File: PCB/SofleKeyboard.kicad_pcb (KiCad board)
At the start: 2 copper layers, 137.2 x 109.2 mm, 87 parts, among them J1 LED, J2 4PIN, J3 OLED, P1 i2c_pin, P2 i2c_pin, SW1 SW_PUSH, SW10 SW_PUSH, SW11 SW_PUSH, SW12 SW_PUSH, SW13 SW_PUSH, SW14 SW_PUSH, SW15 SW_PUSH, SW16 SW_PUSH, SW17 SW_PUSH, SW18 SW_PUSH, SW19 SW_PUSH, SW2 SW_PUSH, SW20 SW_PUSH, SW21 SW_PUSH, SW22 SW_PUSH, SW23 SW_PUSH, SW24 SW_PUSH, SW25 Rotary_Encoder_Switch, SW26 SW_PUSH, SW27 SW_PUSH, SW28 SW_PUSH, SW29 SW_PUSH, SW3 SW_PUSH, SW30 SW_PUSH, SW4 SW_PUSH, SW5 SW_PUSH, SW6 SW_PUSH, SW7 SW_PUSH, SW8 SW_PUSH, SW9 SW_PUSH, U1 ProMicro

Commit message: Finishing touches before ordering
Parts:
- moved Ref** 1.70 mm to (96.8, 124.6)
- moved Ref** 1.42 mm to (95.8, 124.5)
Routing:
- net ENCA: track 73.0 -> 69.0 mm
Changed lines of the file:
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@@
     (thickness 1.6)
     (drawings 193)
-    (tracks 1892)
+    (tracks 1886)
     (zones 0)
     (modules 87)
@@
     (0 F.Cu signal)
     (31 B.Cu signal)
-    (32 B.Adhes user hide)
-    (33 F.Adhes user hide)
-    (34 B.Paste user hide)
-    (35 F.Paste user hide)
+    (32 B.Adhes user)
+    (33 F.Adhes user)
+    (34 B.Paste user)
+    (35 F.Paste user)
     (36 B.SilkS user)
     (37 F.SilkS user)
-    (38 B.Mask user hide)
-    (39 F.Mask user hide)
-    (40 Dwgs.User user hide)
-    (41 Cmts.User user hide)
-    (42 Eco1.User user hide)
+    (38 B.Mask user)
+    (39 F.Mask user)
+    (40 Dwgs.User user)
+    (41 Cmts.User user)
+    (42 Eco1.User user)
     (43 Eco2.User user)
     (44 Edge.Cuts user)
-    (45 Margin user hide)
-    (46 B.CrtYd user hide)
-    (47 F.CrtYd user hide)
-    (48 B.Fab user hide)
-    (49 F.Fab user hide)
+    (45 Margin user)
+    (46 B.CrtYd user)
+    (47 F.CrtYd user)
+    (48 B.Fab user)
+    (49 F.Fab user)
   )
   (setup
@@
   )
   (module SofleKeyboard-footprint:SofleLogoSmall (layer B.Cu)
-    (at 96.58 125.74 180)
+    (at 95.81 124.55 180)
     (fp_text reference Ref** (at 0 0) (layer B.SilkS) hide
       (effects (font (size 1.27 1.27) (thickness 0.15)) (justify mirror))
@@
   )
   (module SofleKeyboard-footprint:SofleLogoSmall (layer F.Cu)
-    (at 97.92 125.86)
+    (at 96.77 124.61)
     (fp_text reference Ref** (at 0 0) (layer F.SilkS) hide
       (effects (font (size 1.27 1.27) (thickness 0.15)))
@@
   (segment (start 98.514255 52.585745) (end 106.224255 52.585745) (width 0.25) (layer F.Cu) (net 56))
   (via (at 98.514255 52.585745) (size 0.4) (drill 0.3) (layers F.Cu B.Cu) (net 56))
-  (segment (start 93.499999 101.000001) (end 92.5 102) (width 0.25) (layer B.Cu) (net 56) (status 20))
+  (segment (start 93.499999 101.000001) (end 92.5 102) (width 0.25) (layer B.Cu) (net 56))
   (segment (start 101.37501 93.12499) (end 93.499999 101.000001) (width 0.25) (layer B.Cu) (net 56))
-  (segment (start 101.37501 87.263295) (end 101.37501 93.12499) (width 0.25) (layer B.Cu) (net 56))
-  (segment (start 98.913295 86.57499) (end 100.686705 86.57499) (width 0.25) (layer B.Cu) (net 56))
-  (segment (start 99.013275 86.47501) (end 98.913295 86.57499) (width 0.25) (layer B.Cu) (net 56))
-  (segment (start 101.37501 85.786705) (end 100.686705 86.47501) (width 0.25) (layer B.Cu) (net 56))
-  (segment (start 101.37501 84.563295) (end 101.37501 85.786705) (width 0.25) (layer B.Cu) (net 56))
-  (segment (start 98.216499 81.404784) (end 101.37501 84.563295) (width 0.25) (layer B.Cu) (net 56))
-  (segment (start 100.686705 86.57499) (end 101.37501 87.263295) (width 0.25) (layer B.Cu) (net 56))
-  (segment (start 98.216499 53.166343) (end 98.216499 81.404784) (width 0.25) (layer B.Cu) (net 56))
   (segment (start 98.514255 52.868587) (end 98.216499 53.166343) (width 0.25) (layer B.Cu) (net 56))
-  (segment (start 100.686705 86.47501) (end 99.013275 86.47501) (width 0.25) (layer B.Cu) (net 56))
   (segment (start 98.514255 52.585745) (end 98.514255 52.868587) (width 0.25) (layer B.Cu) (net 56))
+  (segment (start 98.216499 53.166343) (end 98.216499 81.404784) (width 0.25) (layer B.Cu) (net 56))
+  (segment (start 101.37501 84.563295) (end 101.37501 93.12499) (width 0.25) (layer B.Cu) (net 56))
+  (segment (start 98.216499 81.404784) (end 101.37501 84.563295) (width 0.25) (layer B.Cu) (net 56))
   (segment (start 102.3 80.7) (end 102.7 80.3) (width 0.25) (layer F.Cu) (net 57) (status 30))
   (segment (start 100.2 85.3) (end 99.8 85.3) (width 0.25) (layer B.Cu) (net 57) (status 30))

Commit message: Moving bottom row
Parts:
- moved SW30 10.4 mm to (177.6, 123.8)
- moved SW27 9.84 mm to (118.2, 128.3), turned to 20 degrees
- moved SW29 9.60 mm to (158.6, 122.4)
- moved SW28 9.50 mm to (139.5, 123.8)
- moved SW26 9.04 mm to (97.6, 133.5)
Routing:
- net (no net): track 0.00 -> 3.54 mm, vias 0 -> 1
- net col0: track 358.0 -> 354.5 mm, vias 11 -> 10
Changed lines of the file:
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@@
-(kicad_pcb (version 20171130) (host pcbnew 5.1.4-e60b266~84~ubuntu19.04.1)
+(kicad_pcb (version 20171130) (host pcbnew 5.1.5-52549c5~84~ubuntu19.04.1)
   (general
     (thickness 1.6)
@@
   (layers
     (0 F.Cu signal)
-    (31 B.Cu signal)
-    (32 B.Adhes user)
-    (33 F.Adhes user)
-    (34 B.Paste user)
+    (31 B.Cu signal hide)
+    (32 B.Adhes user hide)
+    (33 F.Adhes user hide)
+    (34 B.Paste user hide)
     (35 F.Paste user)
-    (36 B.SilkS user)
+    (36 B.SilkS user hide)
     (37 F.SilkS user)
-    (38 B.Mask user)
+    (38 B.Mask user hide)
     (39 F.Mask user)
-    (40 Dwgs.User user)
-    (41 Cmts.User user)
+    (40 Dwgs.User user hide)
+    (41 Cmts.User user hide)
     (42 Eco1.User user)
     (43 Eco2.User user)
     (44 Edge.Cuts user)
-    (45 Margin user)
-    (46 B.CrtYd user)
-    (47 F.CrtYd user)
-    (48 B.Fab user)
-    (49 F.Fab user)
+    (45 Margin user hide)
+    (46 B.CrtYd user hide)
+    (47 F.CrtYd user hide)
+    (48 B.Fab user hide)
+    (49 F.Fab user hide)
   )
   (setup
@@
     (pad_to_mask_clearance 0.2)
     (aux_axis_origin 0 0)
+    (grid_origin 129.5 116.1)
     (visible_elements FFFDFFFF)
     (pcbplotparams
@@
   )
   (module SofleKeyboard-footprint:CherryMX_KailhLowProfile_Hotswap_1.5 (layer F.Cu)
-    (at 105.96 130.07 300)
+    (at 97.6 133.5 300)
     (fp_text reference SW26 (at 7 8.1 120) (layer F.SilkS) hide
       (effects (font (size 1 1) (thickness 0.15)))
@@
   )
   (module SofleKeyboard-footprint:CherryMX_KailhLowProfile_Hotswap (layer F.Cu)
-    (at 127.88 126.42 15)
-    (fp_text reference SW27 (at 7 8.1 15) (layer F.SilkS) hide
+    (at 118.226361 128.337462 20)
+    (fp_text reference SW27 (at 7 8.1 20) (layer F.SilkS) hide
       (effects (font (size 1 1) (thickness 0.15)))
     )
-    (fp_text value SW_PUSH (at -7.4 -8.1 15) (layer F.Fab) hide
+    (fp_text value SW_PUSH (at -7.4 -8.1 20) (layer F.Fab) hide
       (effects (font (size 1 1) (thickness 0.15)))
     )
@@
     (fp_line (start 6.1 -4.85) (end 6.1 -0.905) (layer F.SilkS) (width 0.15))
     (fp_line (start 6.1 -0.896) (end 2.49 -0.896) (layer F.SilkS) (width 0.15))
-    (pad 1 smd custom (at -7.2 -5.1 15) (size 0.7 1.5) (layers F.Cu F.Paste F.Mask)
+    (pad 1 smd custom (at -7.2 -5.1 20) (size 0.7 1.5) (layers F.Cu F.Paste F.Mask)
       (net 38 col3)
       (options (clearance outline) (anchor rect))
@@
 ) (width 0.1))
       ))
-    (pad 2 smd custom (at 7.2 -5.1 15) (size 0.7 1.5) (layers B.Cu B.Paste B.Mask)
+    (pad 2 smd custom (at 7.2 -5.1 20) (size 0.7 1.5) (layers B.Cu B.Paste B.Mask)
       (net 31 "Net-(D27-Pad2)")
       (options (clearance outline) (anchor rect))
@@
 ) (width 0.1))
       ))
-    (pad 1 smd custom (at -8.5 -2.5 15) (size 0.7 1.5) (layers B.Cu B.Paste B.Mask)
+    (pad 1 smd custom (at -8.5 -2.5 20) (size 0.7 1.5) (layers B.Cu B.Paste B.Mask)
       (net 38 col3)
       (options (clearance outline) (anchor rect))
@@
            (xy 0.3 -1.2) (xy 2.7 -1.2) (xy 2.7 1.2) (xy 0.3 1.2)) (width 0.1))
       ))
-    (pad 2 smd custom (at 8.5 -2.5 15) (size 0.7 1.5) (layers F.Cu F.Paste F.Mask)
+    (pad 2 smd custom (at 8.5 -2.5 20) (size 0.7 1.5) (layers F.Cu F.Paste F.Mask)
       (net 31 "Net-(D27-Pad2)")
       (options (clearance outline) (anchor rect))
@@
            (xy -2.8 -1.2) (xy -0.4 -1.2) (xy -0.4 1.2) (xy -2.8 1.2)) (width 0.1))
       ))
-    (pad "" np_thru_hole circle (at -3.81 -2.540001 195) (size 3 3) (drill 3) (layers *.Cu *.Mask))
-    (pad "" np_thru_hole circle (at -5.08 0 15) (size 1.7 1.7) (drill 1.7) (layers *.Cu *.Mask))
-    (pad "" np_thru_hole circle (at 5.08 0 15) (size 1.7 1.7) (drill 1.7) (layers *.Cu *.Mask))
-    (pad "" np_thru_hole circle (at 5.5 0 105) (size 1.9 1.9) (drill 1.9) (layers *.Cu *.Mask))
-    (pad "" np_thru_hole circle (at -5.5 0 105) (size 1.9 1.9) (drill 1.9) (layers *.Cu *.Mask))
-    (pad "" np_thru_hole circle (at 0 0 105) (size 4 4) (drill 4) (layers *.Cu *.Mask))
-    (pad "" np_thru_hole circle (at 2.54 -5.08 195) (size 3 3) (drill 3) (layers *.Cu *.Mask))
-    (pad "" np_thru_hole circle (at 0 5.9 105) (size 3 3) (drill 3) (layers *.Cu *.Mask))
-    (pad "" np_thru_hole circle (at -5 3.7 105) (size 3 3) (drill 3) (layers *.Cu *.Mask))
-    (pad 2 smd rect (at 2.8 5.9 195) (size 1.9 2) (layers B.Cu B.Paste B.Mask)
+    (pad "" np_thru_hole circle (at -3.81 -2.540001 200) (size 3 3) (drill 3) (layers *.Cu *.Mask))
+    (pad "" np_thru_hole circle (at -5.08 0 20) (size 1.7 1.7) (drill 1.7) (layers *.Cu *.Mask))
+    (pad "" np_thru_hole circle (at 5.08 0 20) (size 1.7 1.7) (drill 1.7) (layers *.Cu *.Mask))
+    (pad "" np_thru_hole circle (at 5.5 0 110) (size 1.9 1.9) (drill 1.9) (layers *.Cu *.Mask))
+    (pad "" np_thru_hole circle (at -5.5 0 110) (size 1.9 1.9) (drill 1.9) (layers *.Cu *.Mask))
+    (pad "" np_thru_hole circle (at 0 0 110) (size 4 4) (drill 4) (layers *.Cu *.Mask))
+    (pad "" np_thru_hole circle (at 2.54 -5.08 200) (size 3 3) (drill 3) (layers *.Cu *.Mask))
+    (pad "" np_thru_hole circle (at 0 5.9 110) (size 3 3) (drill 3) (layers *.Cu *.Mask))
+    (pad "" np_thru_hole circle (at -5 3.7 110) (size 3 3) (drill 3) (layers *.Cu *.Mask))
+    (pad 2 smd rect (at 2.8 5.9 200) (size 1.9 2) (layers B.Cu B.Paste B.Mask)
       (net 31 "Net-(D27-Pad2)"))
-    (pad 1 smd rect (at -8.1 3.7 195) (size 2 2) (layers B.Cu B.Paste B.Mask)
+    (pad 1 smd rect (at -8.1 3.7 200) (size 2 2) (layers B.Cu B.Paste B.Mask)
       (net 38 col3))
-    (pad 1 smd rect (at 8.1 3.7 195) (size 2 2) (layers F.Cu F.Paste F.Mask)
+    (pad 1 smd rect (at 8.1 3.7 200) (size 2 2) (layers F.Cu F.Paste F.Mask)
       (net 38 col3))
-    (pad 2 smd rect (at -2.8 5.9 195) (size 1.8 2) (layers F.Cu F.Paste F.Mask)
+    (pad 2 smd rect (at -2.8 5.9 200) (size 1.8 2) (layers F.Cu F.Paste F.Mask)
       (net 31 "Net-(D27-Pad2)"))
-    (pad "" np_thru_hole circle (at 5 3.7 285) (size 3 3) (drill 3) (layers *.Cu *.Mask))
-    (pad "" np_thru_hole circle (at -2.54 -5.08 195) (size 3 3) (drill 3) (layers *.Cu *.Mask))
-    (pad "" np_thru_hole circle (at 3.81 -2.54 195) (size 3 3) (drill 3) (layers *.Cu *.Mask))
+    (pad "" np_thru_hole circle (at 5 3.7 290) (size 3 3) (drill 3) (layers *.Cu *.Mask))
+    (pad "" np_thru_hole circle (at -2.54 -5.08 200) (size 3 3) (drill 3) (layers *.Cu *.Mask))
+    (pad "" np_thru_hole circle (at 3.81 -2.54 200) (size 3 3) (drill 3) (layers *.Cu *.Mask))
   )
   (module SofleKeyboard-footprint:CherryMX_KailhLowProfile_Hotswap (layer F.Cu)
-    (at 149 123.75)
+    (at 139.5 123.8)
     (fp_text reference SW28 (at 7 8.1) (layer F.SilkS) hide
       (effects (font (size 1 1) (thickness 0.15)))
@@
   )
   (module SofleKeyboard-footprint:CherryMX_KailhLowProfile_Hotswap (layer F.Cu)
-    (at 168.1 123.75)
+    (at 158.6 122.4)
     (fp_text reference SW29 (at 7 8.1) (layer F.SilkS) hide
       (effects (font (size 1 1) (thickness 0.15)))
@@
   )
   (module SofleKeyboard-footprint:CherryMX_KailhLowProfile_Hotswap (layer F.Cu)
-    (at 187.2 127.9)
+    (at 177.6 123.8)
     (fp_text reference SW30 (at 7 8.1) (layer F.SilkS) hide
       (effects (font (size 1 1) (thickness 0.15)))
@@
   (segment (start 178.8 126.444358) (end 178.744358 126.5) (width 0.25) (layer B.Cu) (net 35))
   (segment (start 174.146718 38.354) (end 173.492674 37.699956) (width 0.25) (layer B.Cu) (net 35))
-  (segment (start 178.9 122.8) (end 178.9 125.344358) (width 0.25) (layer B.Cu) (net 35) (status 20))
+  (segment (start 178.9 122.8) (end 178.9 125.344358) (width 0.25) (layer B.Cu) (net 0) (status 20))
   (segment (start 173.492674 37.699956) (end 105.963634 37.699956) (width 0.25) (layer B.Cu) (net 35))
-  (via (at 178.9 122.8) (size 0.4) (drill 0.3) (layers F.Cu B.Cu) (net 35))
-  (segment (start 180 122.8) (end 179 122.8) (width 0.25) (layer F.Cu) (net 35) (status 10))
+  (via (at 178.9 122.8) (size 0.4) (drill 0.3) (layers F.Cu B.Cu) (net 0))
+  (segment (start 180 122.8) (end 179 122.8) (width 0.25) (layer F.Cu) (net 0) (status 10))
   (segment (start 102.675 40.98859) (end 102.675 57.665745) (width 0.25) (layer B.Cu) (net 35))
   (segment (start 105.963634 37.699956) (end 102.675 40.98859) (width 0.25) (layer B.Cu) (net 35))

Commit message: WIP changing the stagger
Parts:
- moved SW11 4.10 mm to (196.5, 75.4)
- moved SW5 4.10 mm to (196.5, 56.5)
- moved SW17 4.10 mm to (196.5, 94.6)
- moved SW23 4.10 mm to (196.5, 113.6)
- moved SW12 2.61 mm to (215.5, 75.4)
- moved SW6 2.61 mm to (215.5, 56.5)
- moved SW18 2.61 mm to (215.5, 94.6)
- moved SW24 2.61 mm to (215.6, 113.6)
- moved SW26 1.80 mm to (95.8, 133.4)
- moved SW15 1.20 mm to (158.5, 83.2)
- moved SW21 1.20 mm to (158.5, 102.2)
- moved SW29 1.20 mm to (158.5, 121.2)
- moved SW3 1.20 mm to (158.5, 45.0)
- moved SW9 1.20 mm to (158.5, 64.1)
- moved SW27 0.33 mm to (117.9, 128.4)
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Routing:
- net col1: track 350.6 -> 195.4 mm, vias 11 -> 1
- net col0: track 354.5 -> 213.9 mm, vias 10 -> 1
- net col3: track 314.7 -> 242.6 mm, vias 11 -> 9
- net col4: track 311.0 -> 250.5 mm, vias 11 -> 9
- net col2: track 334.4 -> 275.1 mm, vias 11 -> 9
- net row4: track 152.5 -> 110.7 mm
- net Net-(D30-Pad2): track 37.0 -> 0.00 mm, vias 2 -> 0
- net Net-(D26-Pad2): track 36.4 -> 0.00 mm, vias 2 -> 0
- net row2: track 165.8 -> 131.9 mm
- net row0: track 138.2 -> 104.3 mm
- net Net-(D27-Pad2): track 32.8 -> 0.00 mm, vias 2 -> 0
- net row3: track 170.1 -> 137.4 mm
- net Net-(D28-Pad2): track 37.1 -> 14.5 mm, vias 2 -> 1
- net Net-(D29-Pad2): track 36.9 -> 14.5 mm, vias 2 -> 0
- net Net-(D5-Pad2): track 27.9 -> 7.92 mm, vias 2 -> 1
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- removed copper zone on B.Cu, net GND
- removed copper zone on F.Cu, net GND
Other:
- outline, holes or cut-outs redrawn

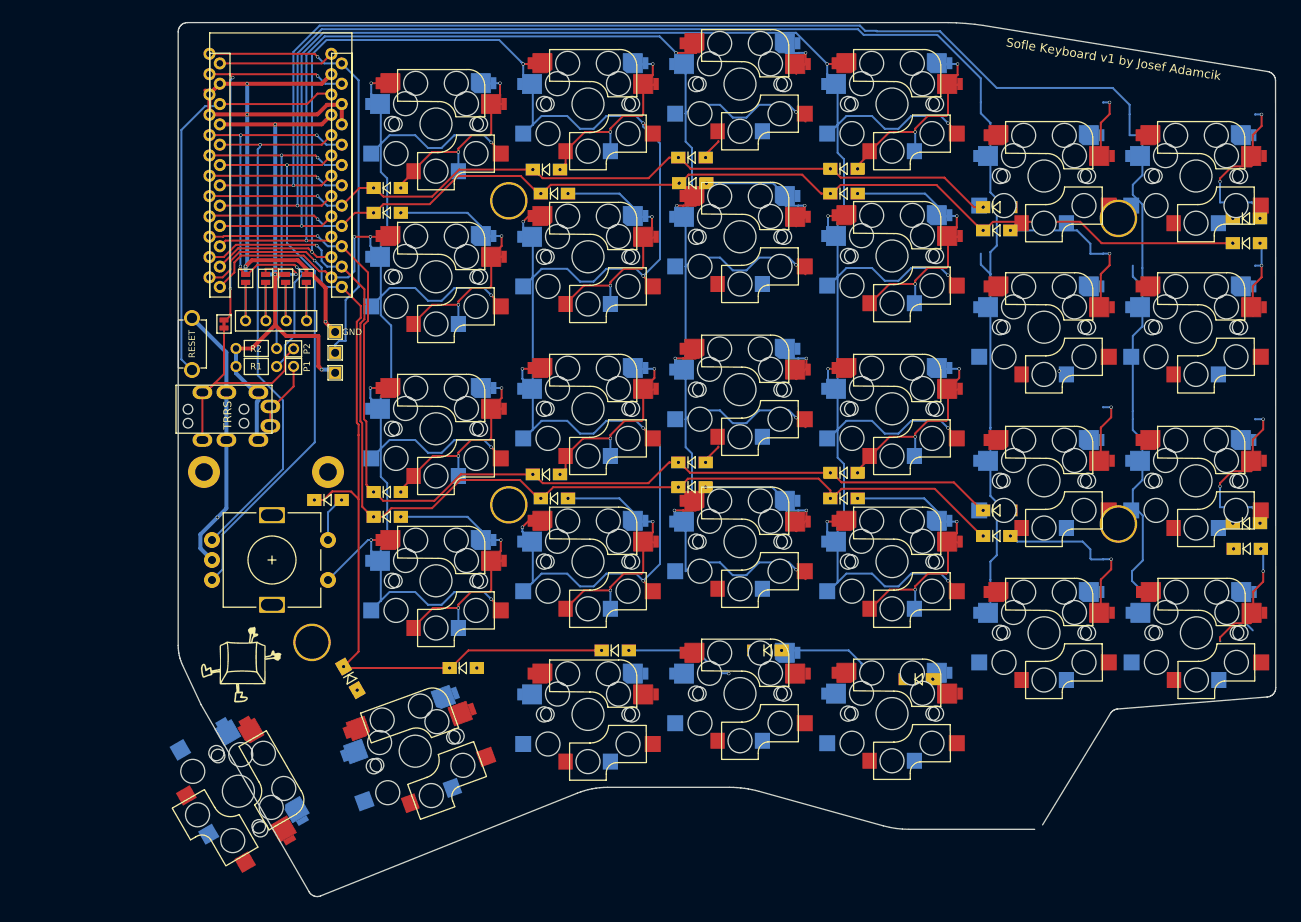
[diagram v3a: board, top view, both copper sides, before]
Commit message: Stagger changed, cleaning and fixing routing for keys
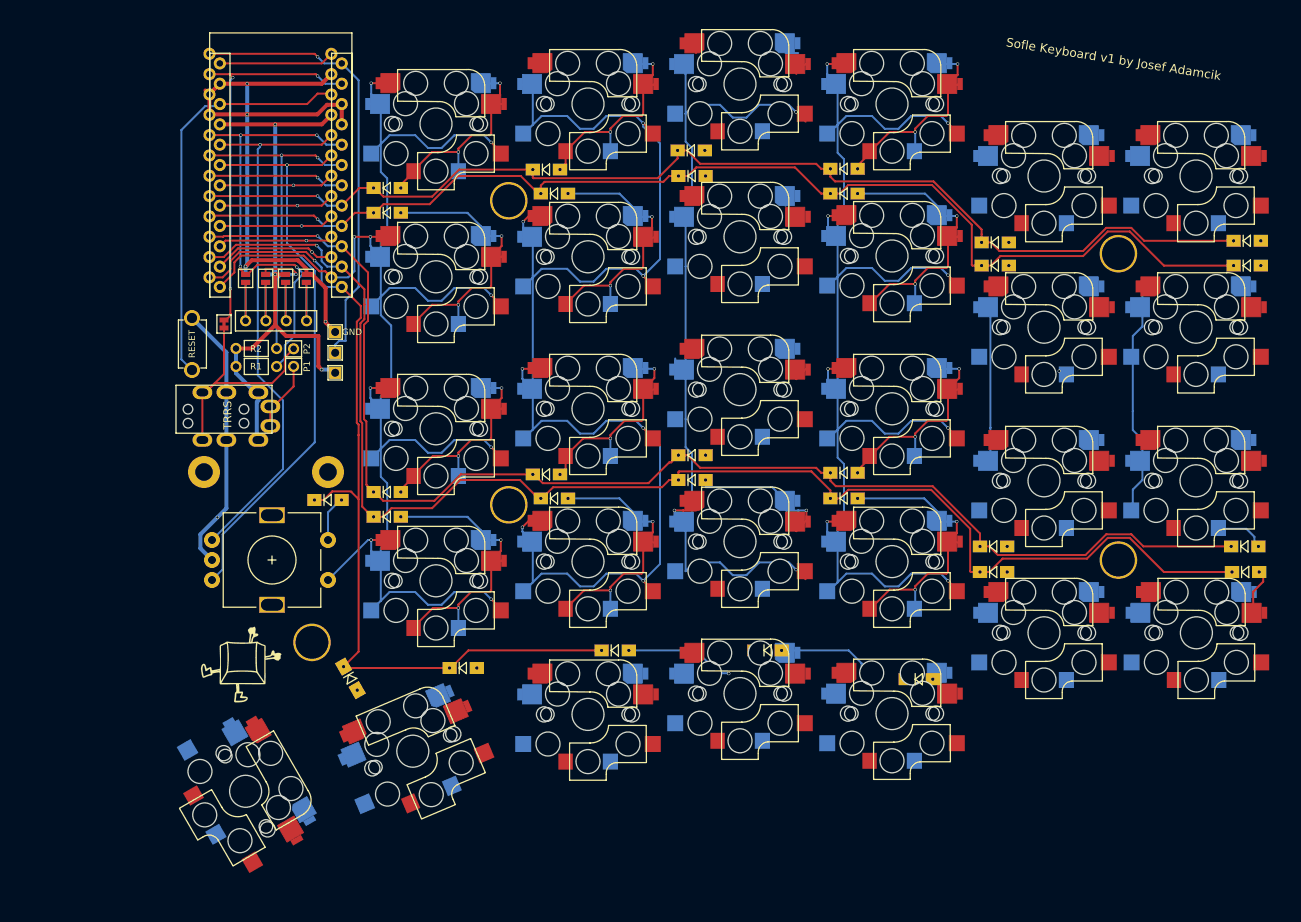
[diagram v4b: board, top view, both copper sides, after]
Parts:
- moved D17 4.52 mm to (190.2, 102.8)
- moved D23 4.52 mm to (190.2, 106.0)
- moved TH6 4.51 mm to (205.8, 104.5)
- moved TH4 4.41 mm to (205.8, 66.2)
- moved D11 4.40 mm to (190.4, 67.7)
- moved D5 4.40 mm to (190.4, 64.8)
- moved D24 2.91 mm to (221.7, 106.0)
- moved D18 2.91 mm to (221.6, 102.8)
- moved D12 2.80 mm to (221.9, 67.7)
- moved D6 2.80 mm to (221.9, 64.6)
- moved D3 0.91 mm to (152.4, 53.3)
- moved D9 0.91 mm to (152.5, 56.5)
- moved SW26 0.90 mm to (96.7, 133.4)
- moved D21 0.90 mm to (152.5, 94.5)
- moved D15 0.90 mm to (152.5, 91.4)
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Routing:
- net col0: track 213.9 -> 43.6 mm
- net col1: track 195.4 -> 33.7 mm
- net col3: track 242.6 -> 124.6 mm, vias 9 -> 4
- net col2: track 275.1 -> 185.2 mm
- net col4: track 250.5 -> 195.2 mm, vias 9 -> 8
- net row3: track 137.4 -> 178.7 mm
- net row0: track 104.3 -> 143.7 mm
- net row2: track 131.9 -> 169.7 mm
- net Net-(D6-Pad2): track 21.9 -> 0.00 mm, vias 2 -> 0
- net Net-(D23-Pad2): track 21.7 -> 0.15 mm, vias 1 -> 0
- net Net-(D11-Pad2): track 21.4 -> 0.28 mm, vias 2 -> 1
- net Net-(D9-Pad2): track 17.3 -> 1.25 mm, vias 1 -> 0
- net Net-(D18-Pad2): track 22.1 -> 6.41 mm, vias 2 -> 0
- net Net-(D12-Pad2): track 10.5 -> 0.28 mm, vias 1 -> 0
- net row1: track 138.3 -> 147.2 mm
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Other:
- board outline removed
